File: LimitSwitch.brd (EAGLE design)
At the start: 17.8 x 25.4 mm, 4 parts

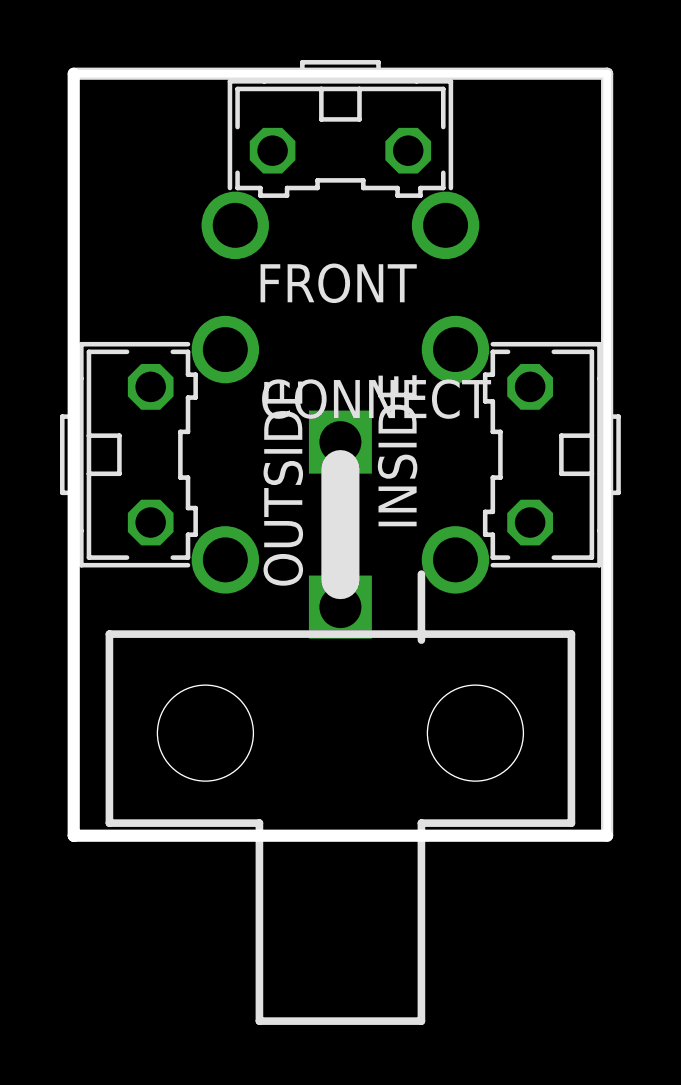
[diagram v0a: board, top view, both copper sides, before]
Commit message: much smaller switch
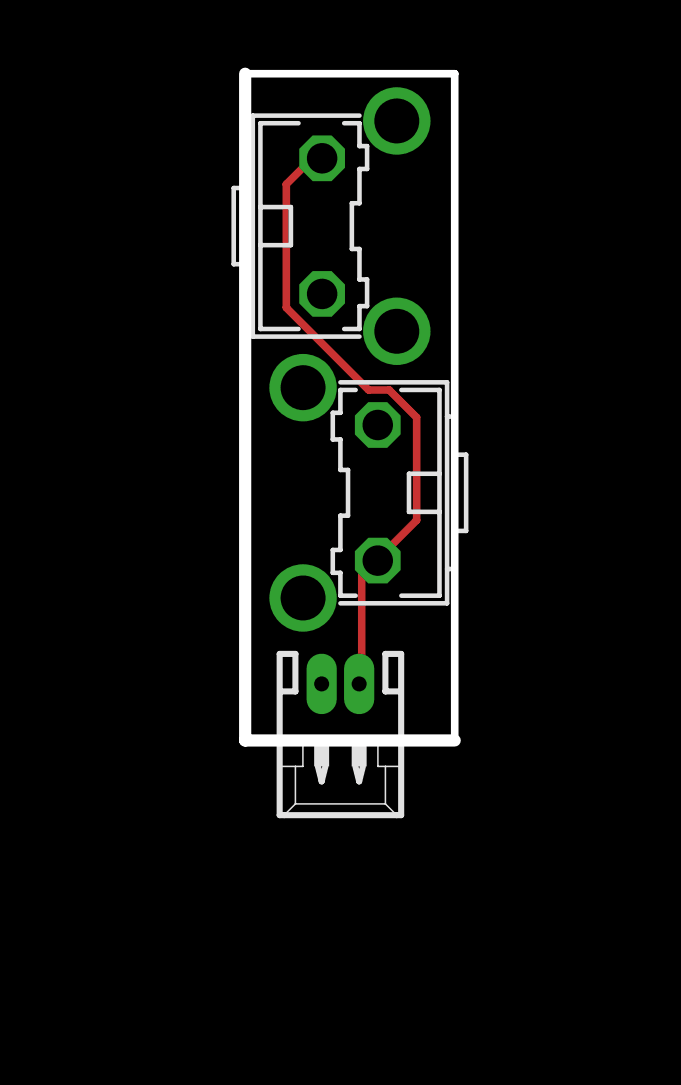
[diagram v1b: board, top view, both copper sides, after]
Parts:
- removed CONNECT: (no value), con-molex-2:5569-2
- removed FRONT: (no value), switch-omron:B3F-31XX
- added X1: 53048-02, con-molex:53048-02
- moved OUTSIDE 9.53 mm to (9.53, 20.3)
- moved INSIDE 5.24 mm to (8.89, 11.4)
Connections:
- net +: now also X1.1; no longer CONNECT.1, FRONT.2
- net GND: now also X1.2; no longer CONNECT.2, FRONT.1
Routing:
- net GND: track 0.00 -> 21.3 mm
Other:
- board size 17.8 x 25.4 mm -> 7 x 22.2 mm
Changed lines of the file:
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@@
 <setting verticaltext="up"/>
 </settings>
-<grid distance="0.05" unitdist="inch" unit="inch" style="lines" multiple="1" display="yes" altdistance="0.025" altunitdist="inch" altunit="inch"/>
+<grid distance="0.025" unitdist="inch" unit="inch" style="lines" multiple="1" display="yes" altdistance="0.025" altunitdist="inch" altunit="inch"/>
 <layers>
 <layer number="1" name="Top" color="4" fill="1" visible="yes" active="yes"/>
@@
 <board>
 <plain>
-<wire x1="17.78" y1="25.4" x2="17.78" y2="0" width="0.4064" layer="21"/>
-<wire x1="0" y1="25.4" x2="17.78" y2="25.4" width="0.4064" layer="21"/>
-<wire x1="0" y1="25.4" x2="0" y2="0" width="0.4064" layer="20"/>
-<wire x1="0" y1="0" x2="17.78" y2="0" width="0.4064" layer="20"/>
-<wire x1="0" y1="25.4" x2="17.78" y2="25.4" width="0.254" layer="20"/>
-<wire x1="17.78" y1="25.4" x2="17.78" y2="0" width="0.254" layer="20"/>
+<wire x1="5.715" y1="25.4" x2="5.715" y2="3.175" width="0.4064" layer="20"/>
+<wire x1="5.715" y1="3.175" x2="12.7" y2="3.175" width="0.4064" layer="20"/>
+<wire x1="5.715" y1="25.4" x2="12.7" y2="25.4" width="0.254" layer="20"/>
+<wire x1="12.7" y1="25.4" x2="12.7" y2="3.175" width="0.254" layer="20"/>
 </plain>
 <attributes>
@@
 </autorouter>
 <elements>
-<element name="CONNECT" library="con-molex-2" package="5569-2" value="" x="8.89" y="7.62"/>
-<element name="FRONT" library="switch-omron" package="B3F-31XX" value="" x="8.89" y="21.59" rot="R180">
-<attribute name="OC_NEWARK" value="36M3582" x="8.89" y="21.59" size="1.778" layer="27" rot="R180" display="off"/>
-<attribute name="MF" value="" x="8.89" y="21.59" size="1.778" layer="27" rot="R180" display="off"/>
-<attribute name="OC_FARNELL" value="959704" x="8.89" y="21.59" size="1.778" layer="27" rot="R180" display="off"/>
-<attribute name="MPN" value="B3F-3100" x="8.89" y="21.59" size="1.778" layer="27" rot="R180" display="off"/>
+<element name="INSIDE" library="switch-omron" package="B3F-31XX" value="" x="8.89" y="11.43" smashed="yes" rot="R90">
+<attribute name="OC_NEWARK" value="36M3582" x="8.89" y="11.43" size="1.778" layer="27" rot="R90" display="off"/>
+<attribute name="MF" value="" x="8.89" y="11.43" size="1.778" layer="27" rot="R90" display="off"/>
+<attribute name="OC_FARNELL" value="959704" x="8.89" y="11.43" size="1.778" layer="27" rot="R90" display="off"/>
+<attribute name="MPN" value="B3F-3100" x="8.89" y="11.43" size="1.778" layer="27" rot="R90" display="off"/>
+<attribute name="VALUE" x="14.859" y="7.747" size="1.27" layer="27" ratio="10" rot="R90"/>
 </element>
-<element name="INSIDE" library="switch-omron" package="B3F-31XX" value="" x="13.97" y="12.7" rot="R90">
-<attribute name="OC_NEWARK" value="36M3582" x="13.97" y="12.7" size="1.778" layer="27" rot="R90" display="off"/>
-<attribute name="MF" value="" x="13.97" y="12.7" size="1.778" layer="27" rot="R90" display="off"/>
-<attribute name="OC_FARNELL" value="959704" x="13.97" y="12.7" size="1.778" layer="27" rot="R90" display="off"/>
-<attribute name="MPN" value="B3F-3100" x="13.97" y="12.7" size="1.778" layer="27" rot="R90" display="off"/>
+<element name="OUTSIDE" library="switch-omron" package="B3F-31XX" value="" x="9.525" y="20.32" smashed="yes" rot="R270">
+<attribute name="OC_NEWARK" value="36M3582" x="9.525" y="20.32" size="1.778" layer="27" rot="R270" display="off"/>
+<attribute name="MF" value="" x="9.525" y="20.32" size="1.778" layer="27" rot="R270" display="off"/>
+<attribute name="OC_FARNELL" value="959704" x="9.525" y="20.32" size="1.778" layer="27" rot="R270" display="off"/>
+<attribute name="MPN" value="B3F-3100" x="9.525" y="20.32" size="1.778" layer="27" rot="R270" display="off"/>
+<attribute name="VALUE" x="3.556" y="24.003" size="1.27" layer="27" ratio="10" rot="R270"/>
 </element>
-<element name="OUTSIDE" library="switch-omron" package="B3F-31XX" value="" x="3.81" y="12.7" rot="R270">
-<attribute name="OC_NEWARK" value="36M3582" x="3.81" y="12.7" size="1.778" layer="27" rot="R270" display="off"/>
-<attribute name="MF" value="" x="3.81" y="12.7" size="1.778" layer="27" rot="R270" display="off"/>
-<attribute name="OC_FARNELL" value="959704" x="3.81" y="12.7" size="1.778" layer="27" rot="R270" display="off"/>
-<attribute name="MPN" value="B3F-3100" x="3.81" y="12.7" size="1.778" layer="27" rot="R270" display="off"/>
+<element name="X1" library="con-molex" package="53048-02" value="53048-02" x="8.89" y="3.81" smashed="yes" rot="R180">
+<attribute name="OC_NEWARK" value="57H4718" x="8.89" y="3.81" size="1.778" layer="27" rot="R180" display="off"/>
+<attribute name="MF" value="MOLEX" x="8.89" y="3.81" size="1.778" layer="27" rot="R180" display="off"/>
+<attribute name="OC_FARNELL" value="1012259" x="8.89" y="3.81" size="1.778" layer="27" rot="R180" display="off"/>
+<attribute name="MPN" value="53048-0210" x="8.89" y="3.81" size="1.778" layer="27" rot="R180" display="off"/>
 </element>
 </elements>
@@
 <signal name="GND">
 <polygon width="0.4064" layer="16">
-<vertex x="0" y="25.4"/>
-<vertex x="0" y="0"/>
-<vertex x="17.78" y="0"/>
-<vertex x="17.78" y="25.4"/>
+<vertex x="5.715" y="25.4"/>
+<vertex x="5.715" y="3.175"/>
+<vertex x="12.7" y="3.175"/>
+<vertex x="12.7" y="25.4"/>
 </polygon>
-<contactref element="CONNECT" pad="2"/>
-<contactref element="FRONT" pad="1"/>
 <contactref element="OUTSIDE" pad="1"/>
 <contactref element="INSIDE" pad="1"/>
+<contactref element="X1" pad="2"/>
+<wire x1="9.6012" y1="8.6868" x2="9.6012" y2="5.2578" width="0.254" layer="1"/>
+<wire x1="10.0584" y1="9.144" x2="9.6012" y2="8.6868" width="0.254" layer="1"/>
+<wire x1="9.6012" y1="5.2578" x2="9.515" y2="5.06" width="0.254" layer="1"/>
+<wire x1="10.0584" y1="9.144" x2="10.1346" y2="9.1694" width="0.254" layer="1"/>
+<wire x1="7.7724" y1="22.4028" x2="8.2296" y2="22.4028" width="0.254" layer="1"/>
+<wire x1="7.0866" y1="21.717" x2="7.7724" y2="22.4028" width="0.254" layer="1"/>
+<wire x1="7.0866" y1="17.6022" x2="7.0866" y2="21.717" width="0.254" layer="1"/>
+<wire x1="9.8298" y1="14.859" x2="7.0866" y2="17.6022" width="0.254" layer="1"/>
+<wire x1="10.5156" y1="14.859" x2="9.8298" y2="14.859" width="0.254" layer="1"/>
+<wire x1="11.43" y1="13.9446" x2="10.5156" y2="14.859" width="0.254" layer="1"/>
+<wire x1="11.43" y1="10.5156" x2="11.43" y2="13.9446" width="0.254" layer="1"/>
+<wire x1="10.287" y1="9.3726" x2="11.43" y2="10.5156" width="0.254" layer="1"/>
+<wire x1="8.2296" y1="22.4028" x2="8.2804" y2="22.5806" width="0.254" layer="1"/>
+<wire x1="10.287" y1="9.3726" x2="10.1346" y2="9.1694" width="0.254" layer="1"/>
 </signal>
 <signal name="+">
 <polygon width="0.4064" layer="1">
-<vertex x="0" y="25.4"/>
-<vertex x="0" y="0"/>
-<vertex x="17.78" y="0"/>
-<vertex x="17.78" y="25.4"/>
+<vertex x="5.715" y="25.4"/>
+<vertex x="5.715" y="3.175"/>
+<vertex x="12.7" y="3.175"/>
+<vertex x="12.7" y="25.4"/>
 </polygon>
-<contactref element="CONNECT" pad="1"/>
-<contactref element="FRONT" pad="2"/>
 <contactref element="OUTSIDE" pad="2"/>
 <contactref element="INSIDE" pad="2"/>
+<contactref element="X1" pad="1"/>
+<wire x1="10.1346" y1="13.6906" x2="8.2804" y2="18.0594" width="0" layer="19" extent="1-1"/>
+<wire x1="8.265" y1="5.06" x2="10.1346" y2="13.6906" width="0" layer="19" extent="1-1"/>
 </signal>
 </signals>

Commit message: sent off an order
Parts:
- removed INSIDE, OUTSIDE: (no value), switch-omron:B3F-31XX
- removed X1: 53048-02, con-molex:53048-02
- added C1: GRM1555C1H471FA01D, resistor:C0402
- added LED1: LG Q396-PS-35, led:CHIPLED_0603
- added R1: ERJ-2RKF1004X, resistor:R0402
- added S2: SKHMPSE010, switch:SKHMPXE010
- added X2: 87438-02, con-molex:87438-02
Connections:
- new net N$1: LED1.C, R1.2
- net +: now also C1.1, LED1.A, S2.1, X2.1; no longer INSIDE.2, OUTSIDE.2, X1.1
- net GND: now also C1.2, R1.1, S2.3, S2.5, X2.2; no longer INSIDE.1, OUTSIDE.1, X1.2
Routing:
- net GND: track 21.3 -> 0.00 mm
- net +: track 0.00 -> 9.57 mm
- net N$1: track 0.00 -> 3.42 mm
- added copper zone on layer 1, net GND
- removed copper zone on layer 1, net +
- removed copper zone on layer 16, net GND
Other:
- board size 7 x 22.2 mm -> 10.1 x 22.5 mm
